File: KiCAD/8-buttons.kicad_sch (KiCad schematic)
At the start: 19 parts, among them U1 74HC165, U2 TLC5916

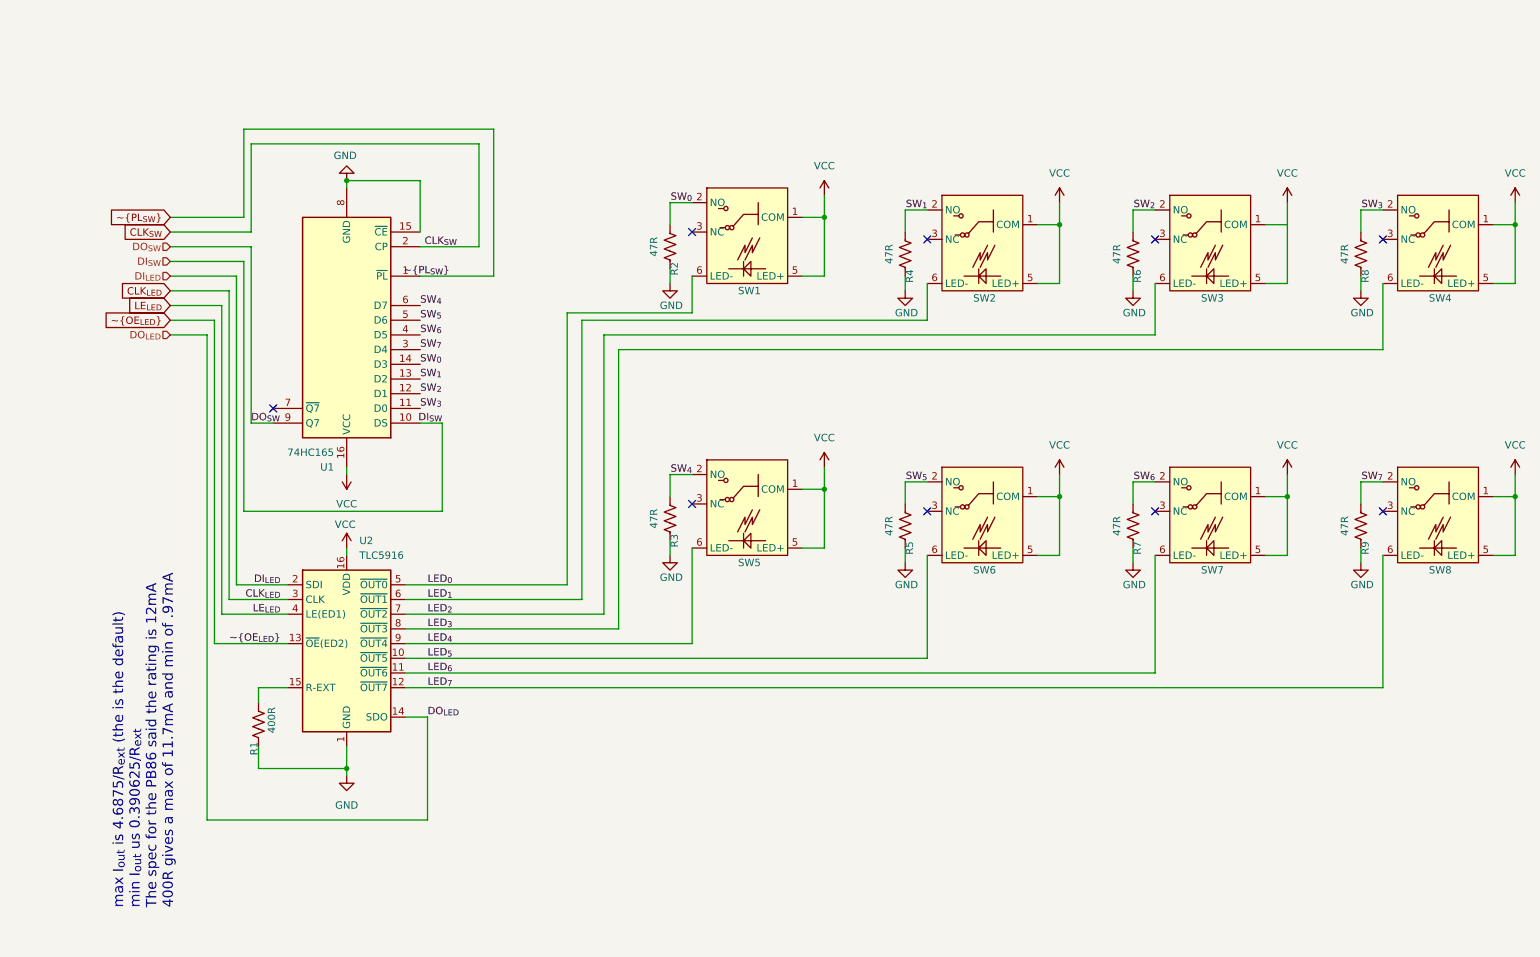
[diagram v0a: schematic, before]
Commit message: reannotate schematic; line things up better
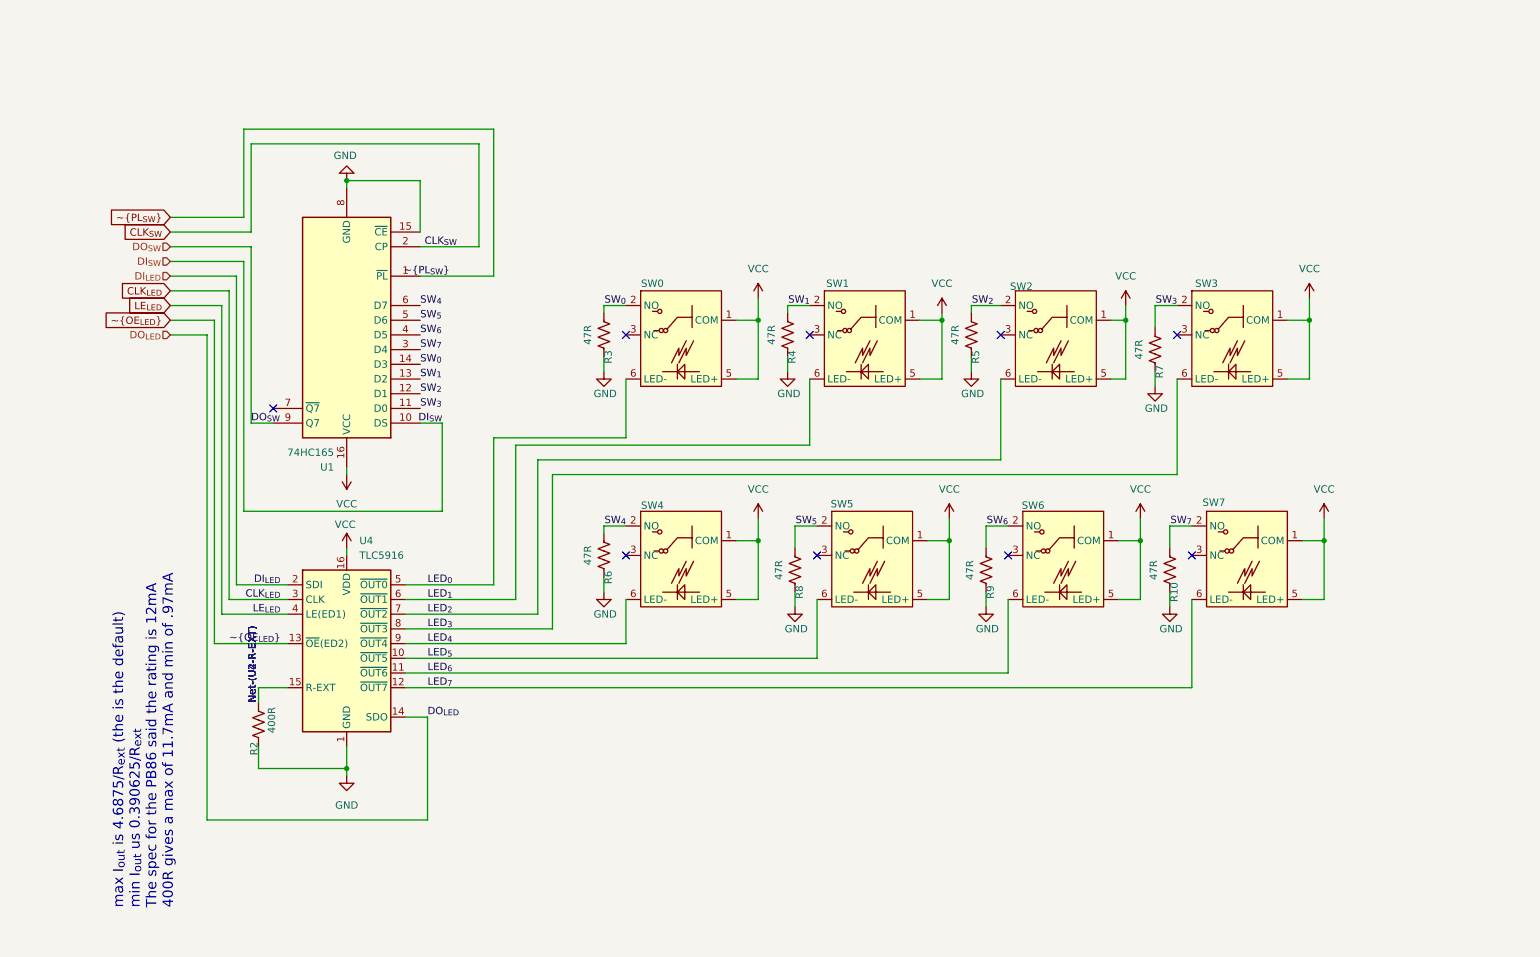
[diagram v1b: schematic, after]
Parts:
- renumbered R9 to R10, R1 to R2, R2 to R3, R6 to R5, R3 to R6, R8 to R7, R5 to R8, R7 to R9, SW1 to SW0, SW3 to SW1, SW5 to SW2, SW7 to SW3, SW2 to SW4, SW4 to SW5, SW8 to SW7, U2 to U4
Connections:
- net Net-(U2-R-EXT): now reaches R2.1, U4.15 (R-EXT)
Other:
- moved on the sheet: R10, R3, R4, R5, R6, R7, R8, R9, SW0, SW1, SW2, SW3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

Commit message: make 3 rows in schema; break single button out to its own kicad_sch
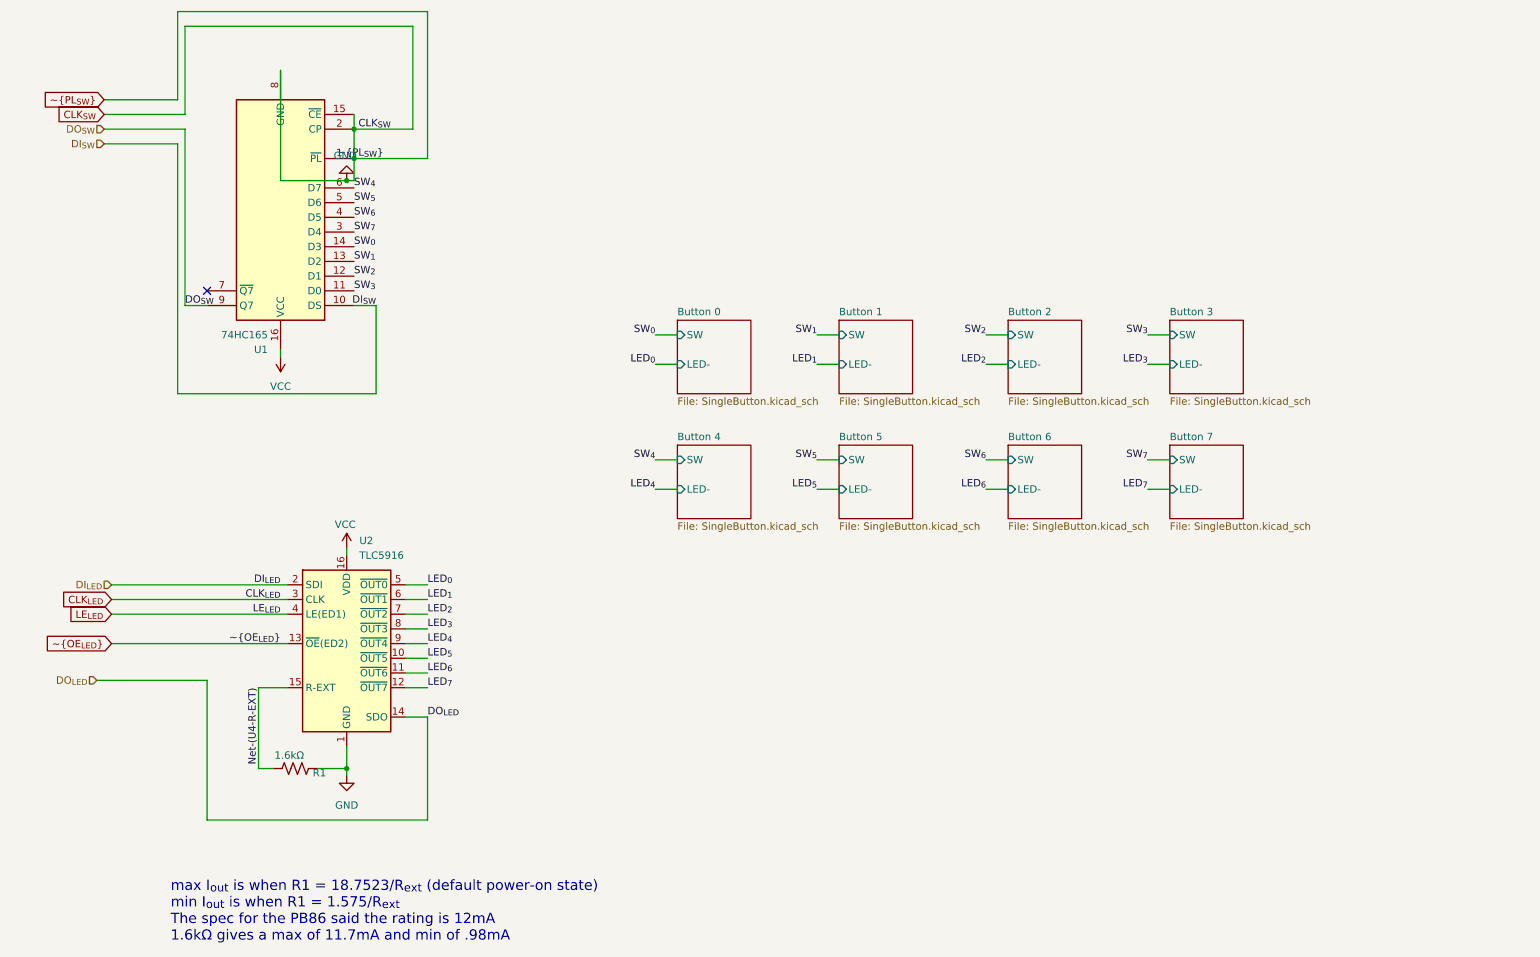
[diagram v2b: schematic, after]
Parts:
- removed R10, R3, R4, R5, R6, R7, R8, R9: 47R, Resistor_THT:R_Axial_DIN0204_L3.6mm_D1.6mm_P5.08mm_Horizontal, symbol Device:R_US
- removed SW0, SW1, SW2, SW3, SW4, SW5, SW6, SW7: ~, Local:PB86, symbol Local:PB68
- R1: renamed from R2; value 400R -> 1.6kΩ; footprint Resistor_THT:R_Axial_DIN0204_L3.6mm_D1.6mm_P5.08mm_Horizontal -> Resistor_SMD:R_0402_1005Metric; LCSC Link (none) -> https://www.lcsc.com/product-detail/Chip-Resistor-Surface-M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; LCSC Part# (none) -> C2906881
- U1: footprint Package_DIP:DIP-16_W7.62mm -> Package_SO:SOIC-16_3.9x9.9mm_P1.27mm; LCSC Link (none) -> https://www.lcsc.com/product-detail/Shift-Registers_Nexperi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; LCSC Part# (none) -> C5613
- U2: renamed from U4; footprint Package_DIP:DIP-16_W7.62mm -> Package_SO:SOIC-16_3.9x9.9mm_P1.27mm; LCSC Link (none) -> https://www.lcsc.com/product-detail/LED-Drivers_Texas-Instr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; LCSC Part# (none) -> C1554191
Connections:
- net CLK_{SW} is gone; now on net GND: U1.2 (CP)
- net ~{PL_{SW}} is gone; now on net GND: U1.1 (~{PL})
- net Net-(U2-R-EXT) renamed Net-(U4-R-EXT)
- no-connect marks 9 -> 1
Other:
- added sheet Button 0 (SingleButton.kicad_sch)
- added sheet Button 1 (SingleButton.kicad_sch)
- added sheet Button 2 (SingleButton.kicad_sch)
- added sheet Button 3 (SingleButton.kicad_sch)
- added sheet Button 4 (SingleButton.kicad_sch)
- added sheet Button 5 (SingleButton.kicad_sch)
- added sheet Button 6 (SingleButton.kicad_sch)
- added sheet Button 7 (SingleButton.kicad_sch)
- moved on the sheet: R1, U1

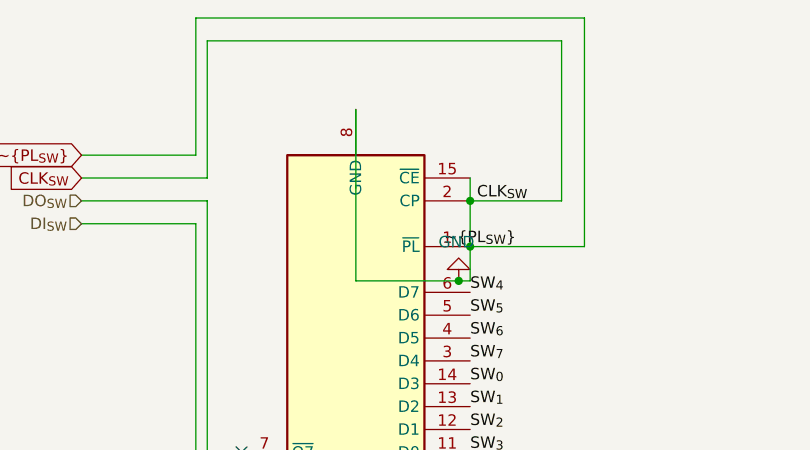
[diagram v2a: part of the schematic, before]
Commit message: fix misplaced wire in schematic
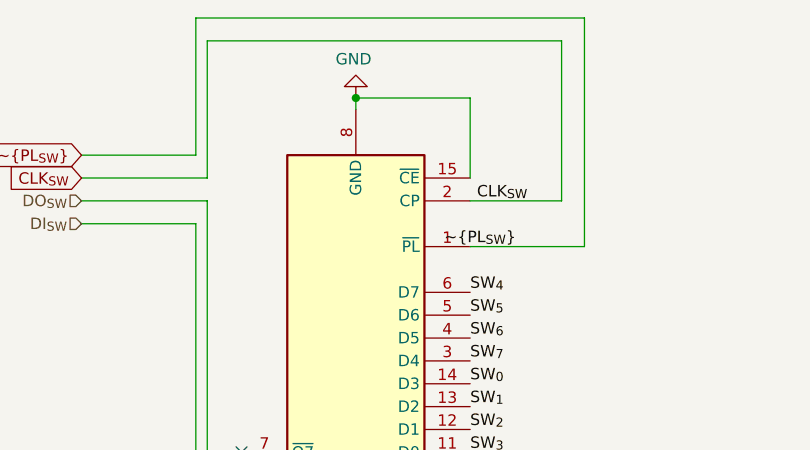
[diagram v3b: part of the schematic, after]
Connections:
- net GND: no longer U1.1 (~{PL}), U1.2 (CP)
- new net CLK_{SW}: U1.2 (CP)
- new net ~{PL_{SW}}: U1.1 (~{PL})
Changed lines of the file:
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@@
 	)
 	(junction
-		(at 69.85 52.07)
-		(diameter 0)
-		(color 0 0 0 0)
-	)
-	(junction
-		(at 71.12 43.18)
-		(diameter 0)
-		(color 0 0 0 0)
-	)
-	(junction
-		(at 71.12 48.26)
+		(at 58.42 31.75)
 		(diameter 0)
 		(color 0 0 0 0)
@@
 	(wire
 		(pts
+			(xy 58.42 31.75) (xy 58.42 33.02)
+		)
+		(stroke
+			(width 0)
+			(type default)
+		)
+	)
+	(wire
+		(pts
 			(xy 151.13 100.33) (xy 154.94 100.33)
 		)
@@
 	(wire
 		(pts
-			(xy 71.12 48.26) (xy 71.12 52.07)
-		)
-		(stroke
-			(width 0)
-			(type default)
-		)
-	)
-	(wire
-		(pts
 			(xy 208.28 78.74) (xy 212.09 78.74)
 		)
@@
 	(wire
 		(pts
-			(xy 58.42 33.02) (xy 58.42 52.07)
-		)
-		(stroke
-			(width 0)
-			(type default)
-		)
-	)
-	(wire
-		(pts
 			(xy 29.21 121.92) (xy 59.69 121.92)
 		)
@@
 	(wire
 		(pts
+			(xy 71.12 31.75) (xy 71.12 40.64)
+		)
+		(stroke
+			(width 0)
+			(type default)
+		)
+	)
+	(wire
+		(pts
 			(xy 123.19 78.74) (xy 127 78.74)
 		)
@@
 	(wire
 		(pts
-			(xy 71.12 52.07) (xy 69.85 52.07)
-		)
-		(stroke
-			(width 0)
-			(type default)
-		)
-	)
-	(wire
-		(pts
 			(xy 80.01 144.78) (xy 83.82 144.78)
 		)
@@
 	(wire
 		(pts
-			(xy 71.12 40.64) (xy 71.12 43.18)
-		)
-		(stroke
-			(width 0)
-			(type default)
-		)
-	)
-	(wire
-		(pts
-			(xy 58.42 52.07) (xy 69.85 52.07)
-		)
-		(stroke
-			(width 0)
-			(type default)
-		)
-	)
-	(wire
-		(pts
 			(xy 80.01 127) (xy 83.82 127)
 		)
@@
 	(wire
 		(pts
+			(xy 58.42 31.75) (xy 71.12 31.75)
+		)
+		(stroke
+			(width 0)
+			(type default)
+		)
+	)
+	(wire
+		(pts
 			(xy 208.28 100.33) (xy 212.09 100.33)
 		)
@@
 		(pts
 			(xy 80.01 139.7) (xy 83.82 139.7)
-		)
-		(stroke
-			(width 0)
-			(type default)
-		)
-	)
-	(wire
-		(pts
-			(xy 71.12 43.18) (xy 71.12 48.26)
 		)
 		(stroke
@@
 	(symbol
 		(lib_id "power:GND")
-		(at 69.85 52.07 180)
+		(at 58.42 31.75 180)
 		(unit 1)
 		(exclude_from_sim no)
@@
 		(dnp no)
 		(property "Reference" "#PWR05"
-			(at 69.85 45.72 0)
+			(at 58.42 25.4 0)
 			(effects
 				(font
@@
 		)
 		(property "Value" "GND"
-			(at 69.596 47.752 0)
+			(at 58.166 27.432 0)
 			(effects
 				(font
@@
 		)
 		(property "Footprint" ""
-			(at 69.85 52.07 0)
+			(at 58.42 31.75 0)
 			(effects
 				(font
@@
 		)
 		(property "Datasheet" ""
-			(at 69.85 52.07 0)
+			(at 58.42 31.75 0)
 			(effects
 				(font
@@
 		)
 		(property "Description" "Power symbol creates a global label with name \"GND\" , ground"
-			(at 69.85 52.07 0)
-			(effects
-				(font
+			(at 58.42 31.75 0)
+			(effects
+				(font

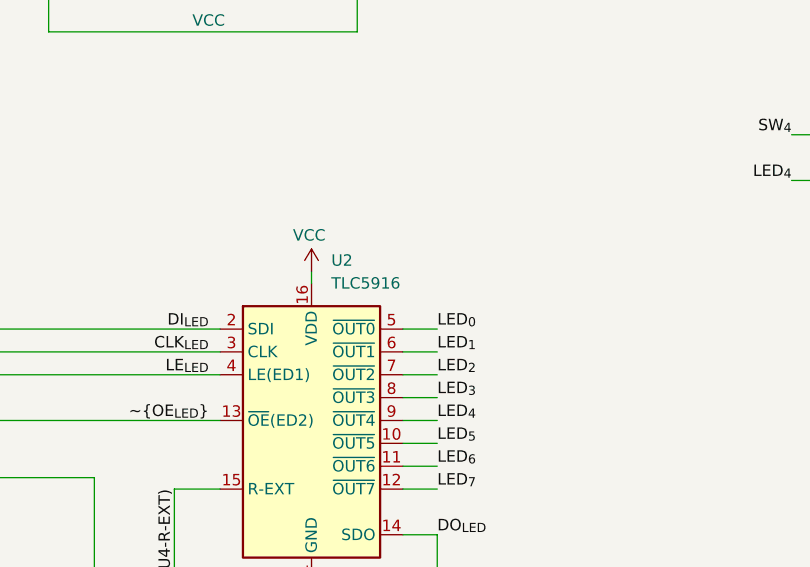
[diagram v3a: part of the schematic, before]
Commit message: DNP for headers; switch 5916->5917
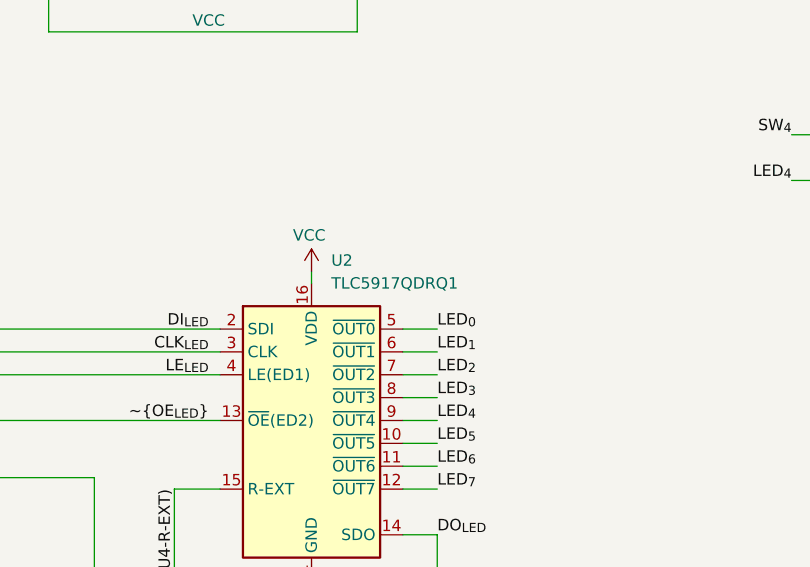
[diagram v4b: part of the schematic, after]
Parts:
- U2: value TLC5916 -> TLC5917QDRQ1; LCSC Link https://www.lcsc.com/product-detail/LED-Drivers_Texas-Instruments-TLC5916ID_C1554191.html?s_z=n_%20TLC5916 -> https://www.lcsc.com/product-detail/LED-Drivers_Texas-Instruments-TLC5917QDRQ1_C2870661.html?s_z=n_TLC5917; LCSC Part# C1554191 -> C2870661
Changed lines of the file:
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@@
 			)
 		)
-		(property "Value" "TLC5916"
+		(property "Value" "TLC5917QDRQ1"
 			(at 72.0441 116.84 0)
 			(effects
@@
 			)
 		)
-		(property "LCSC Link" "https://www.lcsc.com/product-detail/LED-Drivers_Texas-Instruments-TLC5916ID_C1554191.html?s_z=n_%20TLC5916"
+		(property "LCSC Link" "https://www.lcsc.com/product-detail/LED-Drivers_Texas-Instruments-TLC5917QDRQ1_C2870661.html?s_z=n_TLC5917"
 			(at 69.85 132.08 0)
 			(effects
@@
 			)
 		)
-		(property "LCSC Part#" "C1554191"
+		(property "LCSC Part#" "C2870661"
 			(at 69.85 132.08 0)
 			(effects
